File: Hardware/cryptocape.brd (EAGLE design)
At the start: 86.4 x 54.6 mm, 52 parts, among them J1 AVR_SPI_PRG_6PTH, U1 33mhz, U2 ATMEGA328P, U3 EEPROM-I2CSMD, Y2 8MHZ

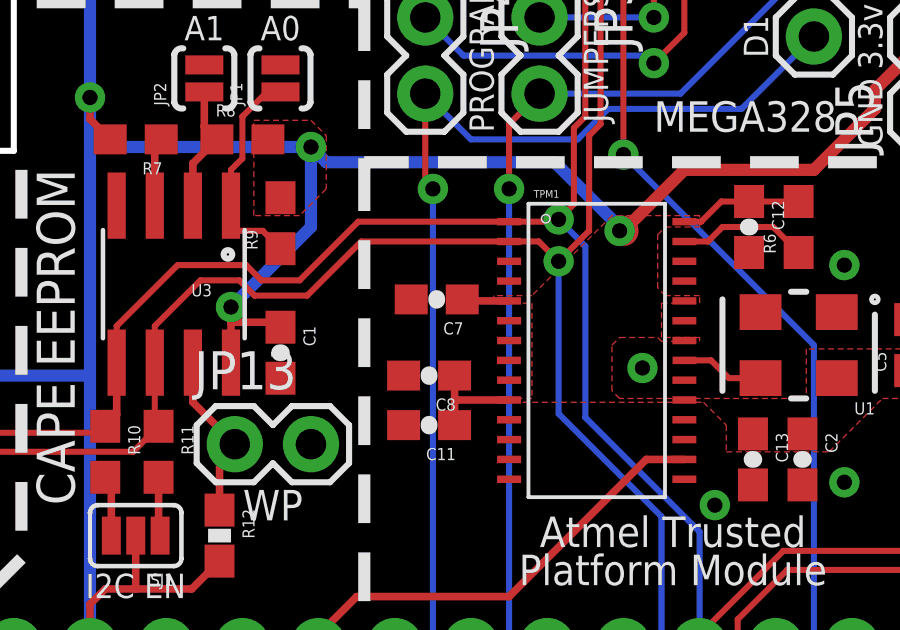
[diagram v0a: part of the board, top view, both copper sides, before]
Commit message: fixed capacitor C7 alignment to match C11
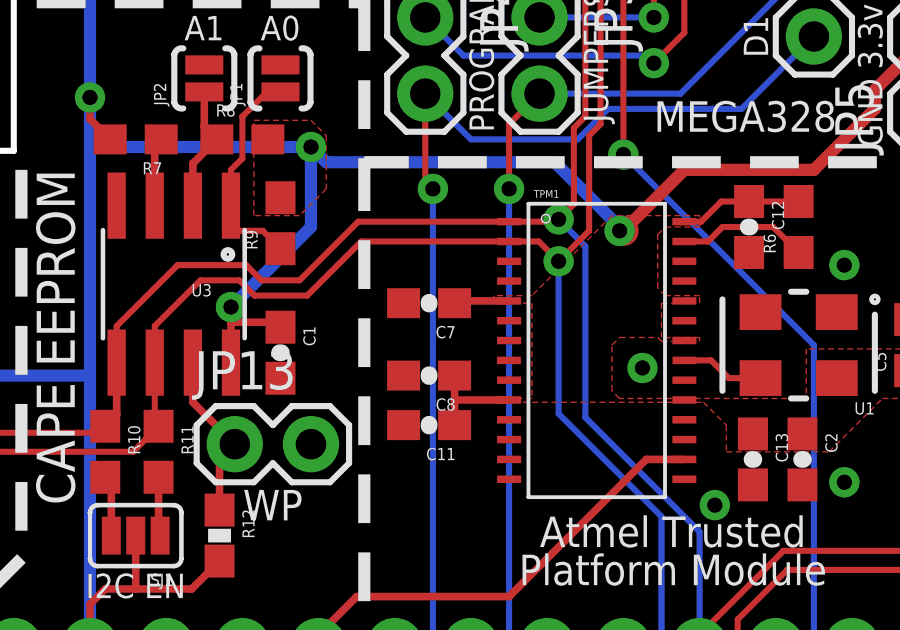
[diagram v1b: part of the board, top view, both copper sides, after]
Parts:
- moved C7 0.28 mm to (34.2, 15.9)
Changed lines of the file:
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@@
 <setting verticaltext="up"/>
 </settings>
-<grid distance="0.01" unitdist="inch" unit="inch" style="lines" multiple="1" display="yes" altdistance="0.005" altunitdist="inch" altunit="inch"/>
+<grid distance="0.005" unitdist="inch" unit="inch" style="lines" multiple="1" display="yes" altdistance="0.005" altunitdist="inch" altunit="inch"/>
 <layers>
 <layer number="1" name="Top" color="4" fill="1" visible="yes" active="yes"/>
@@
 <attribute name="VALUE" value="0.1uF" x="46.609" y="10.668" size="1.778" layer="27" rot="R270" display="off"/>
 </element>
-<element name="C7" library="SparkFun-Capacitors" package="0603-CAP" value="2200pf" x="34.417" y="16.002" rot="R180">
-<attribute name="PROD_ID" value="CAP-07877" x="34.417" y="16.002" size="1.778" layer="27" rot="R180" display="off"/>
-<attribute name="VALUE" value="2.2nF" x="34.417" y="16.002" size="1.778" layer="27" rot="R180" display="off"/>
+<element name="C7" library="SparkFun-Capacitors" package="0603-CAP" value="2200pf" x="34.163" y="15.875" rot="R180">
+<attribute name="PROD_ID" value="CAP-07877" x="34.163" y="15.875" size="1.778" layer="27" rot="R180" display="off"/>
+<attribute name="VALUE" value="2.2nF" x="34.163" y="15.875" size="1.778" layer="27" rot="R180" display="off"/>
 </element>
 <element name="C8" library="SparkFun-Capacitors" package="0603-CAP" value="2200pf" x="34.163" y="13.462" rot="R180">
@@
 <wire x1="35.013" y1="12.6492" x2="35.013" y2="11.811" width="0.254" layer="1"/>
 <wire x1="36.83" y1="12.6492" x2="35.013" y2="12.6492" width="0.254" layer="1"/>
-<wire x1="36.83" y1="15.9512" x2="35.267" y2="15.9512" width="0.254" layer="1"/>
-<wire x1="35.267" y1="15.9512" x2="35.267" y2="16.002" width="0.254" layer="1"/>
+<wire x1="36.83" y1="15.9512" x2="35.14" y2="15.9512" width="0.254" layer="1"/>
+<wire x1="35.14" y1="15.9512" x2="35.013" y2="15.875" width="0.254" layer="1"/>
 <polygon width="0.2032" layer="1">
 <vertex x="36.322" y="16.129"/>

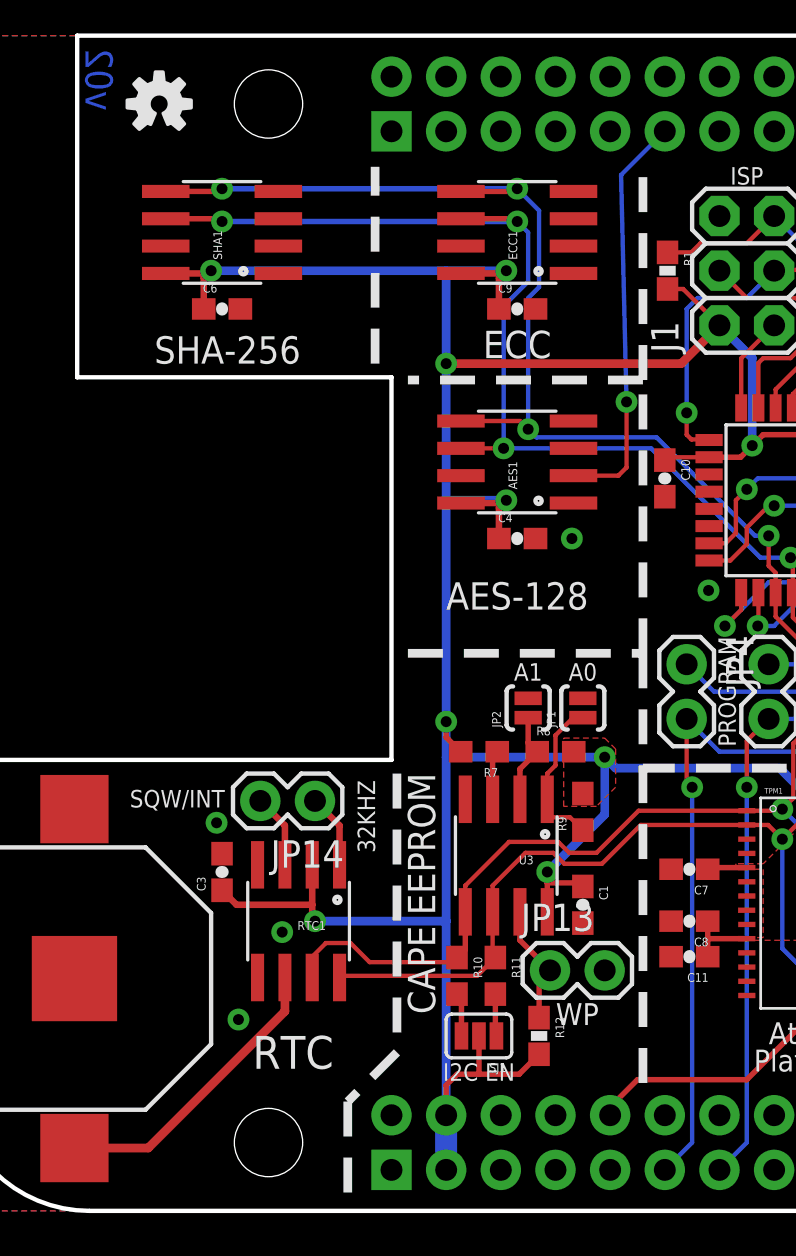
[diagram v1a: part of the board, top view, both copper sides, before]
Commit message: Fixed off angle wire and added TP for RTC battery.
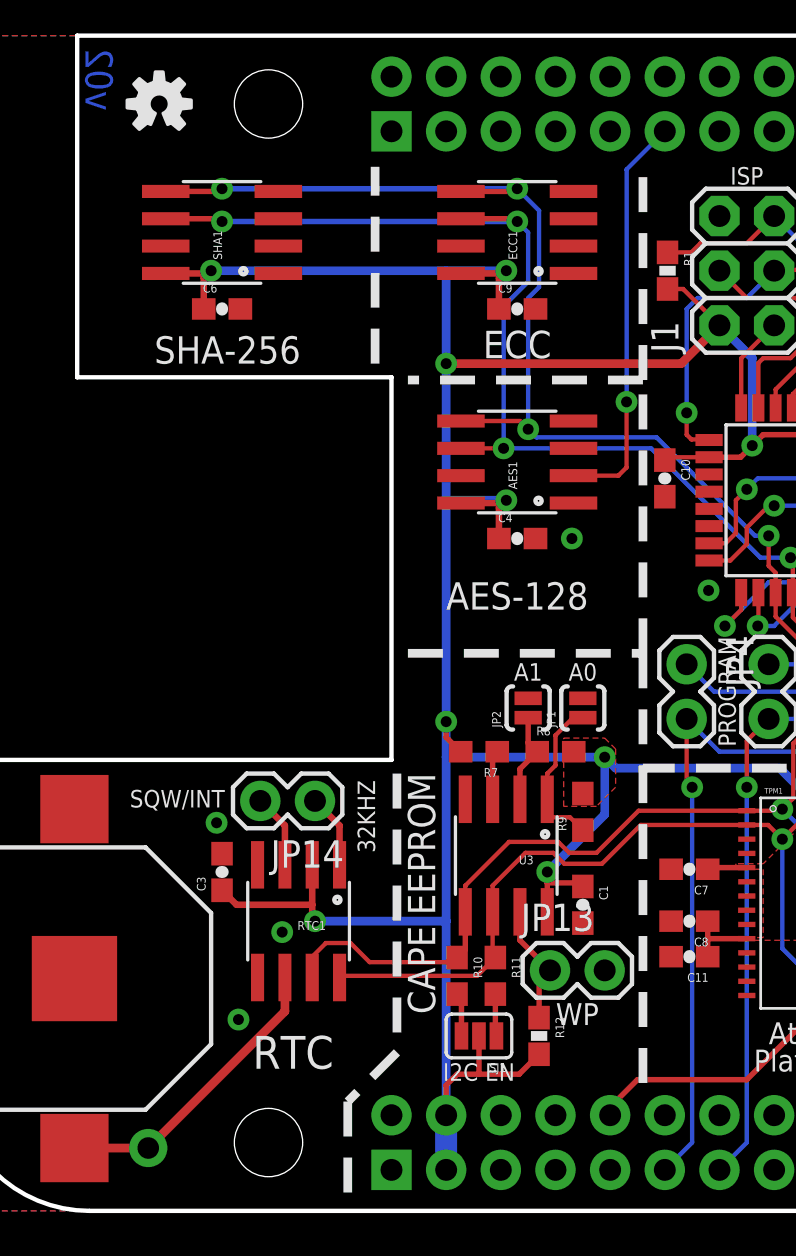
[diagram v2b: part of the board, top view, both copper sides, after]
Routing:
- net VBAT: vias 0 -> 1
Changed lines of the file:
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@@
 <wire x1="15.367" y1="9.271" x2="9.017" y2="2.921" width="0.4064" layer="1"/>
 <wire x1="5.588" y1="2.921" x2="9.017" y2="2.921" width="0.4064" layer="1"/>
+<via x="9.017" y="2.921" extent="1-16" drill="1" diameter="1.778"/>
 </signal>
 <signal name="I2C2_SCL">
@@
 <wire x1="31.242" y1="34.544" x2="31.242" y2="37.592" width="0.2032" layer="1"/>
 <via x="31.242" y="37.592" extent="1-16" drill="0.508"/>
-<wire x1="31.242" y1="37.592" x2="30.988" y2="48.133" width="0.2032" layer="16"/>
-<wire x1="30.988" y1="48.133" x2="33.02" y2="50.165" width="0.2032" layer="16"/>
+<wire x1="31.242" y1="37.592" x2="31.242" y2="48.387" width="0.2032" layer="16"/>
+<wire x1="31.242" y1="48.387" x2="33.02" y2="50.165" width="0.2032" layer="16"/>
 </signal>
 <signal name="N$34">

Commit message: Superficial changes to schematic and board.
- Fixes bent wire on schematic on BBB header.
- Changes "set" to "clear" on EEPROM
- Adds ATATES132 to I2C address list
- Resorts the list by address
- Changes "Atmel Trusted Platform Module" to TPM on brd
- Changes "MEGA328" to "m328P"
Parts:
- JP1: value Sets A0 -> Clears A0
- JP2: value Sets A1 -> Clears A1
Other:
- board text added: "TPM"
- board text added: "m328P"
- board text removed: "Atmel Trusted"
- board text removed: "MEGA328"
- board text removed: "Platform Module"
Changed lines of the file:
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@@
 <text x="28.956" y="9.652" size="1.016" layer="21" font="vector" ratio="16" rot="R180" align="bottom-center">WP</text>
 <text x="28.956" y="9.906" size="1.27" layer="22" font="vector" ratio="16" rot="MR180" align="bottom-center">WP</text>
-<text x="42.291" y="7.747" size="1.016" layer="21" font="vector" ratio="15" align="bottom-center">Atmel Trusted</text>
-<text x="42.291" y="6.477" size="1.016" layer="21" font="vector" ratio="15" align="bottom-center">Platform Module</text>
 <wire x1="50.546" y1="6.096" x2="50.546" y2="11.303" width="0.4064" layer="21" style="shortdash"/>
 <wire x1="50.546" y1="11.303" x2="51.689" y2="11.303" width="0.4064" layer="21" style="shortdash"/>
@@
 <text x="36.322" y="24.13" size="0.8128" layer="22" font="vector" ratio="15" rot="MR270" align="bottom-center">JUMPERS</text>
 <text x="26.162" y="27.94" size="1.27" layer="21" font="vector" ratio="15" align="bottom-center">AES-128</text>
-<text x="44.704" y="22.606" size="1.016" layer="21" font="vector" ratio="15" rot="R180" align="bottom-center">MEGA328</text>
+<text x="44.704" y="22.606" size="1.016" layer="21" font="vector" ratio="15" rot="R180" align="bottom-center">m328P</text>
 <text x="51.816" y="9.525" size="0.8128" layer="21" font="vector" ratio="15" rot="R90" align="bottom-center">SDA</text>
 <text x="51.816" y="6.985" size="0.8128" layer="21" font="vector" ratio="15" rot="R90" align="bottom-center">SCL</text>
@@
 <text x="6.096" y="52.578" size="1.27" layer="16" font="vector" ratio="15" rot="MR90" align="bottom-center">v02</text>
 <text x="50.8" y="-9.652" size="1.778" layer="51" ratio="15" rot="R180" align="bottom-right">Josh Datko / Casey Kuhns</text>
+<text x="42.291" y="6.477" size="1.524" layer="21" font="vector" ratio="15" align="bottom-center">TPM</text>
 </plain>
 <attributes>
@@
 <attribute name="PROD_ID" value="RES-07857" x="3.81" y="13.462" size="1.778" layer="27" rot="R90" display="off"/>
 </element>
-<element name="JP2" library="SparkFun-Passives" package="SJ_2S-NO" value="Sets A1" x="26.67" y="23.368" rot="R90"/>
-<element name="JP1" library="SparkFun-Passives" package="SJ_2S-NO" value="Sets A0" x="29.21" y="23.368" rot="R90"/>
+<element name="JP2" library="SparkFun-Passives" package="SJ_2S-NO" value="Clears A1" x="26.67" y="23.368" rot="R90"/>
+<element name="JP1" library="SparkFun-Passives" package="SJ_2S-NO" value="Clears A0" x="29.21" y="23.368" rot="R90"/>
 <element name="C1" library="SparkFun-Capacitors" package="0603-CAP" value="0.1u" x="29.21" y="14.224" rot="R270">
 <attribute name="PROD_ID" value="CAP-00810" x="44.45" y="100.584" size="1.778" layer="27" rot="R270" display="off"/>
